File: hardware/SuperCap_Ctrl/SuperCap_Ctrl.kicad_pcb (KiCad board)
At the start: 2 copper layers, 45 x 45 mm, 89 parts, among them J1 Conn_01x02, J2 Conn_01x04, J3 Conn_01x32_MountingPin, J4 Conn_01x03, Q1 Si2308, Q3 Si2308, Q4 Si2308, Q5 Si2308, Q6 Si2308, U1 STM32G474VCTx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

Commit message: wip: before subtree sync
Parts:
- moved R7 3.20 mm to (124.6, 108.8)
- moved R9 3.10 mm to (120.2, 108.8), turned to 180 degrees
- moved Q3 1.42 mm to (122.4, 107.2), turned to -90 degrees
- moved Q4 1.16 mm to (122.4, 103.3), turned to -90 degrees
- moved Q5 1.15 mm to (118.0, 107.2), turned to -90 degrees
- moved R10 0.93 mm to (118.0, 100.5), turned to 0 degrees
- moved R8 0.93 mm to (122.3, 100.5), turned to 0 degrees
- moved Q6 0.82 mm to (118.0, 103.3), turned to -90 degrees
- moved C13 0.30 mm to (127.8, 84.9)
- moved D7 0.20 mm to (117.1, 106.5)
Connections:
- Q1 pad 2: Net-(D1-A) -> GND
- Q1 pad 3: GND -> Net-(D1-A)
- Q3 pad 2: Net-(D6-K2) -> Net-(Q3-D)
- Q3 pad 3: Net-(Q3-D) -> Net-(D6-K2)
- Q4 pad 2: Net-(D6-K1) -> Net-(Q4-D)
- Q4 pad 3: Net-(Q4-D) -> Net-(D6-K1)
- Q5 pad 2: Net-(D7-K2) -> Net-(Q5-D)
- Q5 pad 3: Net-(Q5-D) -> Net-(D7-K2)
- Q6 pad 2: Net-(D7-K1) -> Net-(Q6-D)
- Q6 pad 3: Net-(Q6-D) -> Net-(D7-K1)
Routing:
- net +3.3V: track 138.4 -> 141.6 mm
- net LED_A2: track 6.46 -> 3.34 mm
- net LED_B1: track 4.43 -> 6.93 mm
- net Net-(D1-A): track 6.74 -> 8.51 mm
- net Net-(D7-K2): track 2.15 -> 0.67 mm
- net Net-(D7-K1): track 2.15 -> 0.73 mm
- net LED_A1: track 4.90 -> 6.14 mm
- net Net-(Q6-D): track 2.60 -> 1.84 mm
- net Net-(Q5-D): track 3.33 -> 2.71 mm
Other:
- board text added: "WEILAI_SuperCap_Ctrl_v0.2"
- board text removed: "WEILAI_SuperCap_Ctrl_v0.1"

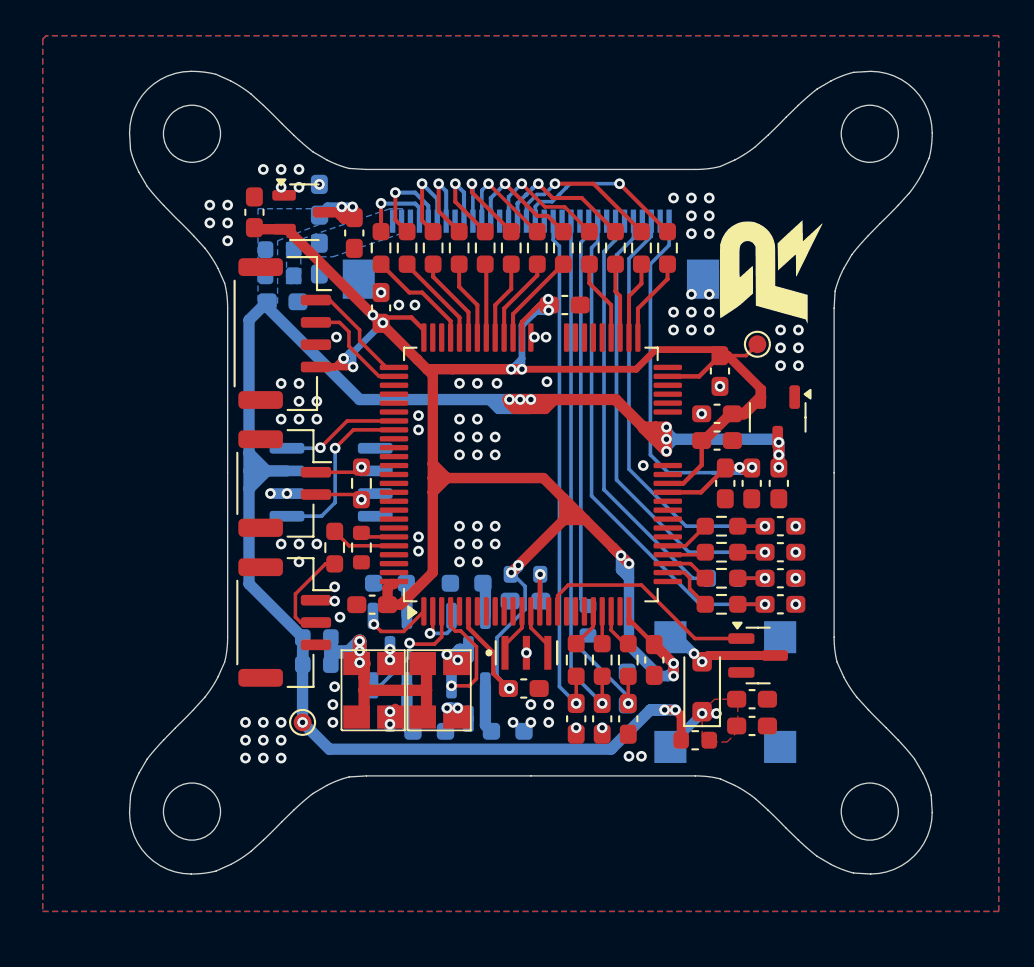
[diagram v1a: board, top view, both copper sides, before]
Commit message: 修改LED电路
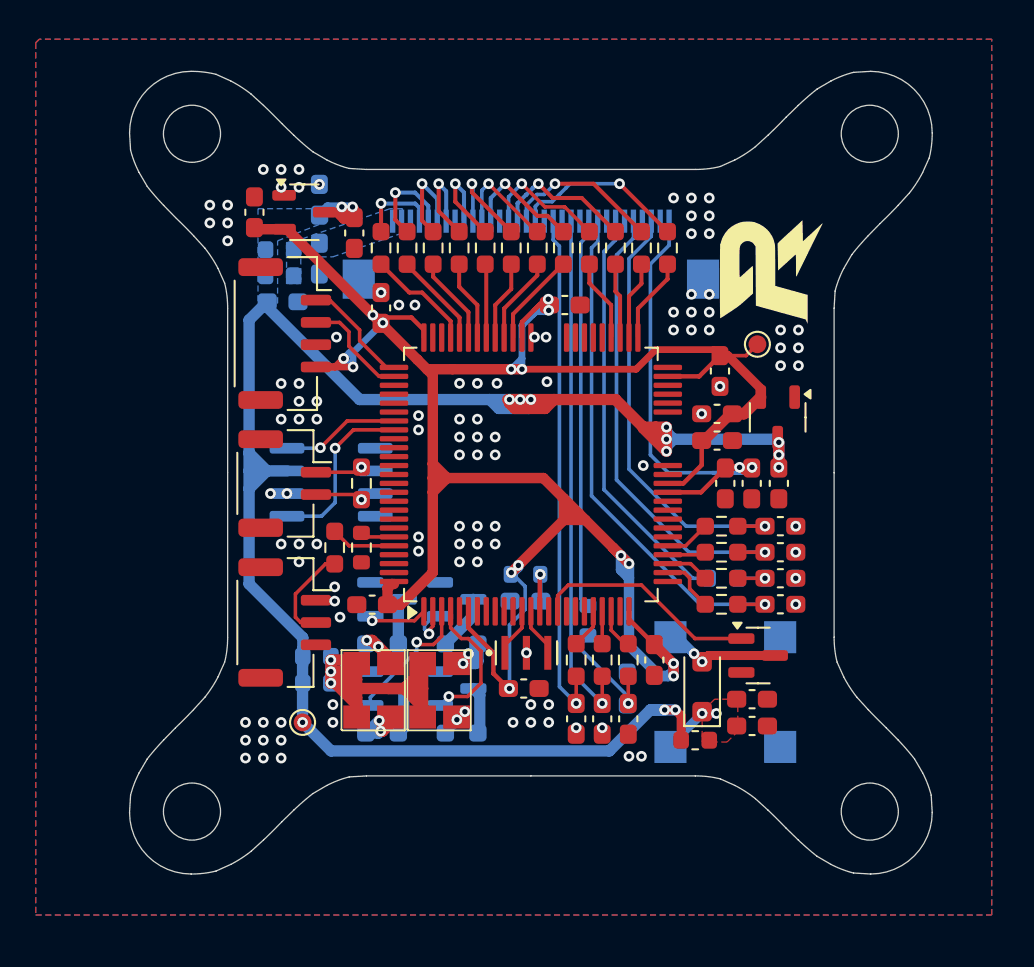
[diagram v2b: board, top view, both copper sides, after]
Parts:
- moved R10 3.43 mm to (117.6, 103.9), turned to 180 degrees
- moved R8 3.41 mm to (122.0, 103.9)
- moved R9 2.64 mm to (117.6, 108.9)
- moved R7 2.58 mm to (122.0, 108.9)
- moved Q4 1.98 mm to (121.7, 101.4), turned to 0 degrees
- moved Q6 1.87 mm to (117.8, 101.4), turned to 0 degrees
- moved FB6 1.05 mm to (113.9, 104.6)
- moved FB7 1.05 mm to (113.9, 106.1)
- moved Q3 1.01 mm to (121.7, 106.4), turned to 0 degrees
- moved Q5 0.78 mm to (117.8, 106.4), turned to 0 degrees
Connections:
- Q3 pad 2: Net-(Q3-D) -> GND
- Q3 pad 3: Net-(D6-K2) -> Net-(Q3-S)
- Q4 pad 2: Net-(Q4-D) -> GND
- Q4 pad 3: Net-(D6-K1) -> Net-(Q4-S)
- Q5 pad 2: Net-(Q5-D) -> GND
- Q5 pad 3: Net-(D7-K2) -> Net-(Q5-S)
- Q6 pad 2: Net-(Q6-D) -> GND
- Q6 pad 3: Net-(D7-K1) -> Net-(Q6-S)
- R10 pad 1: GND -> Net-(Q6-S)
- R10 pad 2: Net-(Q6-D) -> Net-(D7-K1)
- R7 pad 1: GND -> Net-(Q3-S)
- R7 pad 2: Net-(Q3-D) -> Net-(D6-K2)
- R8 pad 1: GND -> Net-(Q4-S)
- R8 pad 2: Net-(Q4-D) -> Net-(D6-K1)
- R9 pad 1: GND -> Net-(Q5-S)
- R9 pad 2: Net-(Q5-D) -> Net-(D7-K2)
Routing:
- net Net-(D6-A1): track 16.9 -> 30.5 mm
- net Net-(Q4-S): track 0.00 -> 3.15 mm
- net Net-(D7-K2): track 0.67 -> 3.70 mm
- net Net-(Q3-D): track 2.71 -> 0.00 mm
- net Net-(Q5-D): track 2.71 -> 0.00 mm
- net Net-(Q3-S): track 0.00 -> 2.69 mm
- net Net-(Q6-S): track 0.00 -> 2.63 mm
- net Net-(Q5-S): track 0.00 -> 2.63 mm
- net Net-(D7-K1): track 0.73 -> 3.09 mm
- net Net-(Q4-D): track 1.88 -> 0.00 mm
- net Net-(Q6-D): track 1.84 -> 0.00 mm
- net LED_A1: track 6.14 -> 7.78 mm
- net LED_B1: track 6.93 -> 7.67 mm
- net Net-(D6-K2): track 2.90 -> 2.25 mm
- net Net-(D6-K1): track 3.17 -> 3.81 mm
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
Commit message: 修改LED电路_1
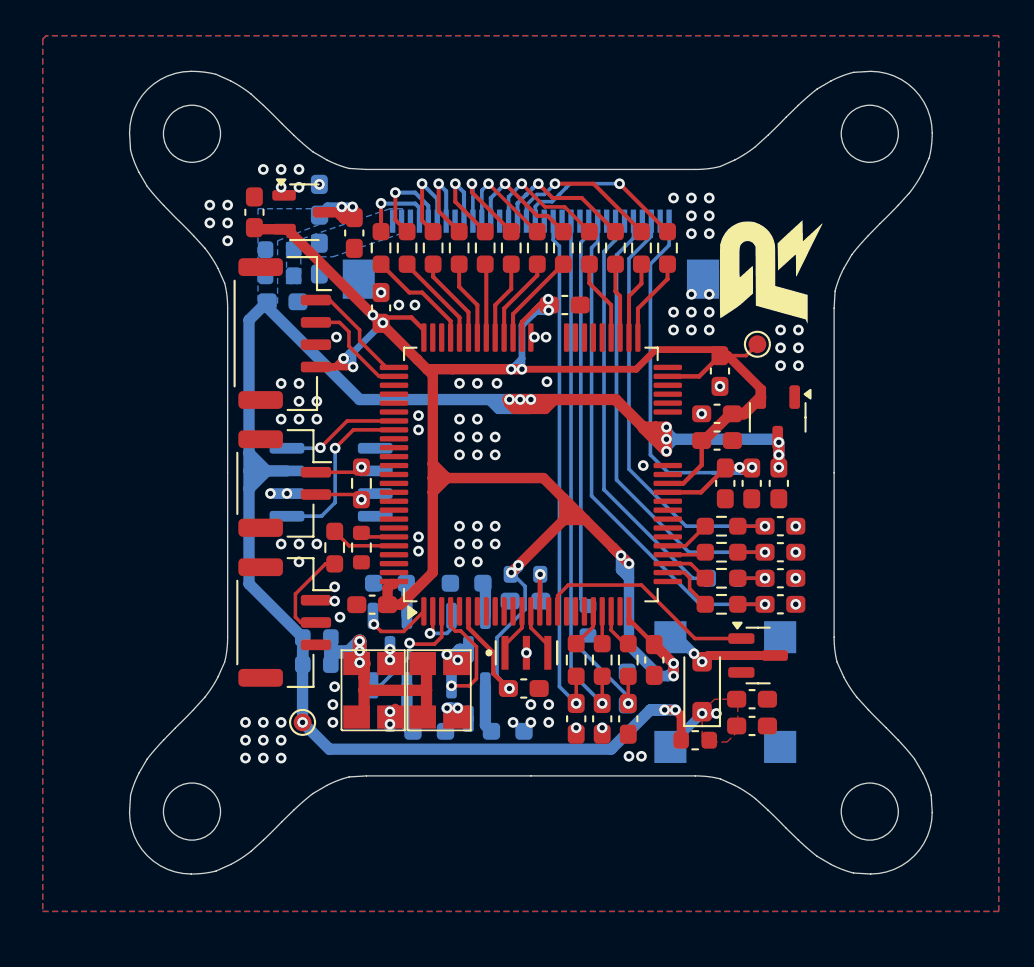
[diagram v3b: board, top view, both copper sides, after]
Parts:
- moved R10 3.43 mm to (118.0, 100.5), turned to 0 degrees
- moved R8 3.41 mm to (122.3, 100.5)
- moved R9 2.64 mm to (120.2, 108.8)
- moved R7 2.58 mm to (124.6, 108.8)
- moved Q4 1.98 mm to (122.4, 103.3), turned to -90 degrees
- moved Q6 1.87 mm to (118.0, 103.3), turned to -90 degrees
- moved FB6 1.05 mm to (113.9, 103.5)
- moved FB7 1.05 mm to (113.9, 105.0)
- moved Q3 1.01 mm to (122.4, 107.2), turned to -90 degrees
- moved Q5 0.78 mm to (118.0, 107.2), turned to -90 degrees
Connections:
- Q3 pad 2: GND -> Net-(Q3-D)
- Q3 pad 3: Net-(Q3-S) -> Net-(D6-K2)
- Q4 pad 2: GND -> Net-(Q4-D)
- Q4 pad 3: Net-(Q4-S) -> Net-(D6-K1)
- Q5 pad 2: GND -> Net-(Q5-D)
- Q5 pad 3: Net-(Q5-S) -> Net-(D7-K2)
- Q6 pad 2: GND -> Net-(Q6-D)
- Q6 pad 3: Net-(Q6-S) -> Net-(D7-K1)
- R10 pad 1: Net-(Q6-S) -> GND
- R10 pad 2: Net-(D7-K1) -> Net-(Q6-D)
- R7 pad 1: Net-(Q3-S) -> GND
- R7 pad 2: Net-(D6-K2) -> Net-(Q3-D)
- R8 pad 1: Net-(Q4-S) -> GND
- R8 pad 2: Net-(D6-K1) -> Net-(Q4-D)
- R9 pad 1: Net-(Q5-S) -> GND
- R9 pad 2: Net-(D7-K2) -> Net-(Q5-D)
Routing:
- net Net-(D6-A1): track 30.5 -> 16.9 mm
- net Net-(Q4-S): track 3.15 -> 0.00 mm
- net Net-(D7-K2): track 3.70 -> 0.67 mm
- net Net-(Q3-D): track 0.00 -> 2.71 mm
- net Net-(Q5-D): track 0.00 -> 2.71 mm
- net Net-(Q3-S): track 2.69 -> 0.00 mm
- net Net-(Q6-S): track 2.63 -> 0.00 mm
- net Net-(Q5-S): track 2.63 -> 0.00 mm
- net Net-(D7-K1): track 3.09 -> 0.73 mm
- net Net-(Q4-D): track 0.00 -> 1.88 mm
- net Net-(Q6-D): track 0.00 -> 1.84 mm
- net LED_A1: track 7.78 -> 6.14 mm
- net LED_B1: track 7.67 -> 6.93 mm
- net Net-(D6-K2): track 2.25 -> 2.90 mm
- net Net-(D6-K1): track 3.81 -> 3.17 mm
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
